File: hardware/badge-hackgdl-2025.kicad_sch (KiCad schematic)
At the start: 53 parts, among them J1 ADDON, J2 Battery, P1 USB_C_Plug_USB2.0, Q1 DMG3415U-7, Q2 MMBT2222A, SW1 ON, SW2 RESET, SW3 BOOT, SW4 RIGHT, SW5 BACK, SW6 LEFT, SW7 MIDDLE, U1 XC6220B331MR-G, U2 ESP32-S3-WROOM-1-N16

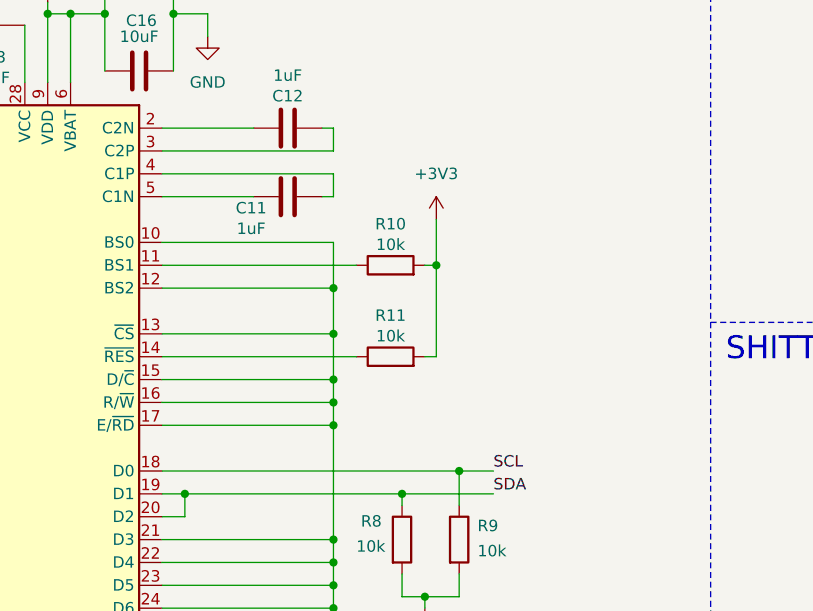
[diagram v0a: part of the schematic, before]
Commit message: feat(hw): add capacitor in reset pin
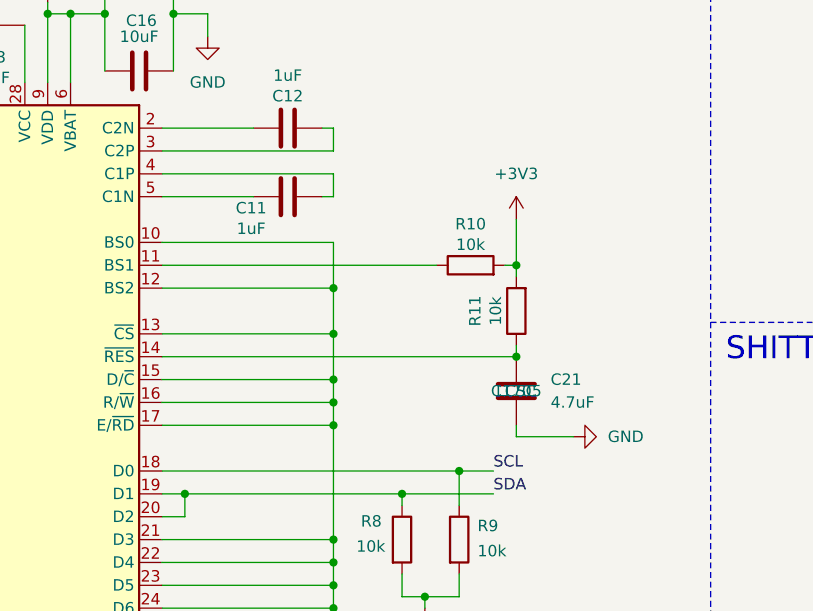
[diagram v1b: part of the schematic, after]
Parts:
- added C21: 4.7uF, Capacitor_SMD:C_0603_1608Metric, symbol Device:C
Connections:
- net GND: now also C21.2
- net at DS1.14 (~{RES}), R11.1: now also C21.1
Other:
- moved on the sheet: R10, R11
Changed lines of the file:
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@@
 	)
 	(junction
+		(at 93.98 129.54)
+		(diameter 0)
+		(color 0 0 0 0)
+	)
+	(junction
 		(at 229.87 96.52)
 		(diameter 0)
@@
 	)
 	(junction
-		(at 85.09 129.54)
-		(diameter 0)
-		(color 0 0 0 0)
-	)
-	(junction
 		(at 104.14 48.26)
 		(diameter 0)
@@
 	)
 	(junction
+		(at 93.98 139.7)
+		(diameter 0)
+		(color 0 0 0 0)
+	)
+	(junction
 		(at 41.91 190.5)
 		(diameter 0)
@@
 	(wire
 		(pts
+			(xy 93.98 129.54) (xy 93.98 130.81)
+		)
+		(stroke
+			(width 0)
+			(type default)
+		)
+	)
+	(wire
+		(pts
 			(xy 44.45 190.5) (xy 44.45 185.42)
 		)
@@
 	(wire
 		(pts
-			(xy 54.61 129.54) (xy 76.2 129.54)
+			(xy 54.61 129.54) (xy 85.09 129.54)
 		)
 		(stroke
@@
 	(wire
 		(pts
+			(xy 93.98 148.59) (xy 100.33 148.59)
+		)
+		(stroke
+			(width 0)
+			(type default)
+		)
+	)
+	(wire
+		(pts
 			(xy 78.74 46.99) (xy 78.74 45.72)
 		)
@@
 	(wire
 		(pts
-			(xy 85.09 129.54) (xy 83.82 129.54)
+			(xy 93.98 129.54) (xy 92.71 129.54)
 		)
 		(stroke
@@
 	(wire
 		(pts
-			(xy 85.09 124.46) (xy 85.09 129.54)
+			(xy 93.98 124.46) (xy 93.98 129.54)
 		)
 		(stroke
@@
 	(wire
 		(pts
-			(xy 54.61 139.7) (xy 76.2 139.7)
+			(xy 54.61 139.7) (xy 93.98 139.7)
 		)
 		(stroke
@@
 	(wire
 		(pts
+			(xy 93.98 138.43) (xy 93.98 139.7)
+		)
+		(stroke
+			(width 0)
+			(type default)
+		)
+	)
+	(wire
+		(pts
 			(xy 163.83 19.812) (xy 163.83 20.32)
 		)
@@
 	(wire
 		(pts
-			(xy 85.09 139.7) (xy 85.09 129.54)
-		)
-		(stroke
-			(width 0)
-			(type default)
-		)
-	)
-	(wire
-		(pts
 			(xy 54.61 147.32) (xy 73.66 147.32)
 		)
@@
 	(wire
 		(pts
-			(xy 83.82 139.7) (xy 85.09 139.7)
+			(xy 93.98 148.59) (xy 93.98 147.32)
 		)
 		(stroke
@@
 	(symbol
 		(lib_id "Device:R")
-		(at 80.01 139.7 90)
+		(at 93.98 134.62 180)
 		(unit 1)
 		(exclude_from_sim no)
@@
 		(dnp no)
 		(property "Reference" "R11"
-			(at 80.01 135.128 90)
+			(at 89.408 134.62 90)
 			(effects
 				(font
@@
 		)
 		(property "Value" "10k"
-			(at 80.01 137.414 90)
+			(at 91.694 134.62 90)
 			(effects
 				(font
@@
 		)
 		(property "Footprint" "Resistor_SMD:R_0603_1608Metric"
-			(at 80.01 141.478 90)
+			(at 95.758 134.62 90)
 			(effects
 				(font
@@
 		)
 		(property "Datasheet" "~"
-			(at 80.01 139.7 0)
+			(at 93.98 134.62 0)
 			(effects
 				(font
@@
 		)
 		(property "Description" "Resistor"
-			(at 80.01 139.7 0)
+			(at 93.98 134.62 0)
 			(effects
 				(font
@@
 		)
 		(property "LCSC#" "C99198"
-			(at 80.01 139.7 0)
+			(at 93.98 134.62 0)
 			(effects
 				(font
@@
 		)
 		(property "provedor" "LCSC"
-			(at 80.01 139.7 0)
+			(at 93.98 134.62 0)
 			(effects
 				(font
@@
 		(lib_name "+3V3_3")
 		(lib_id "power:+3V3")
-		(at 85.09 124.46 0)
+		(at 93.98 124.46 0)
 		(unit 1)
 		(exclude_from_sim no)
@@
 		(fields_autoplaced yes)
 		(property "Reference" "#PWR034"
-			(at 85.09 128.27 0)
+			(at 93.98 128.27 0)
 			(effects
 				(font
@@
 		)
 		(property "Value" "+3V3"
-			(at 85.09 119.38 0)
+			(at 93.98 119.38 0)
 			(effects
 				(font
@@
 		)
 		(property "Footprint" ""
-			(at 85.09 124.46 0)
+			(at 93.98 124.46 0)
 			(effects
 				(font
@@
 		)
 		(property "Datasheet" ""
-			(at 85.09 124.46 0)
+			(at 93.98 124.46 0)
 			(effects
 				(font
@@
 		)
 		(property "Description" "Power symbol creates a global label with name \"+3V3\""
-			(at 85.09 124.46 0)
+			(at 93.98 124.46 0)
 			(effects
 				(font
@@
 	)
 	(symbol
+		(lib_id "Device:C")
+		(at 93.98 143.51 0)
+		(unit 1)
+		(exclude_from_sim no)
+		(in_bom yes)
+		(on_board yes)
+		(dnp no)
+		(fields_autoplaced yes)
+		(property "Reference" "C21"
+			(at 97.79 142.2399 0)
+			(effects
+				(font
+					(size 1.27 1.27)
+				)
+				(justify left)
+			)
+		)
+		(property "Value" "4.7uF"
+			(at 97.79 144.7799 0)
+			(effects
+				(font
+					(size 1.27 1.27)
+				)
+				(justify left)
+			)
+		)
+		(property "Footprint" "Capacitor_SMD:C_0603_1608Metric"
+			(at 94.9452 147.32 0)
+			(effects
+				(font
+					(size 1.27 1.27)
+				)
+				(hide yes)
+			)
+		)
+		(property "Datasheet" "~"
+			(at 93.98 143.51 0)
+			(effects
+				(font
+					(size 1.27 1.27)
+				)
+				(hide yes)
+			)
+		)
+		(property "Description" "Unpolarized capacitor"
+			(at 93.98 143.51 0)
+			(effects
+				(font
+					(size 1.27 1.27)
+				)
+				(hide yes)
+			)
+		)
+		(property "LCSC#" "C1705"
+			(at 93.98 143.51 0)
+			(effects
+				(font
+					(size 1.27 1.27)
+				)
+			)
+		)
+		(property "provedor" "LCSC"
+			(at 93.98 143.51 0)
+			(effects
+				(font
+					(size 1.27 1.27)
+				)
+			)
+		)
+		(pin "2"
+		)
+		(pin "1"
+		)
+		(instances
+			(project ""
+				(path "/570c3069-5a6c-4b3e-98ab-959d221dff05"
+					(reference "C21")
+					(unit 1)
+				)
+			)
+		)
+	)
+	(symbol
 		(lib_id "power:GND")
 		(at 163.83 26.162 0)
@@
 	)
 	(symbol
+		(lib_name "GND_10")
+		(lib_id "power:GND")
+		(at 100.33 148.59 90)
+		(unit 1)
+		(exclude_from_sim no)
+		(in_bom yes)
+		(on_board yes)
+		(dnp no)
+		(fields_autoplaced yes)
+		(property "Reference" "#PWR049"
+			(at 106.68 148.59 0)
+			(effects
+				(font
+					(size 1.27 1.27)
+				)
+				(hide yes)
+			)
+		)
+		(property "Value" "GND"
+			(at 104.14 148.5899 90)
+			(effects
+				(font
+					(size 1.27 1.27)
+				)
+				(justify right)
+			)
+		)
+		(property "Footprint" ""
+			(at 100.33 148.59 0)
+			(effects
+				(font
+					(size 1.27 1.27)
+				)
+				(hide yes)
+			)
+		)
+		(property "Datasheet" ""
+			(at 100.33 148.59 0)
+			(effects
+				(font
+					(size 1.27 1.27)
+				)
+				(hide yes)
+			)
+		)
+		(property "Description" "Power symbol creates a global label with name \"GND\" , ground"
+			(at 100.33 148.59 0)
+			(effects
+				(font
+					(size 1.27 1.27)
+				)
+				(hide yes)
+			)
+		)
+		(pin "1"
+		)
+		(instances
+			(project ""
+				(path "/570c3069-5a6c-4b3e-98ab-959d221dff05"
+					(reference "#PWR049")
+					(unit 1)
+				)
+			)
+		)
+	)
+	(symbol
 		(lib_id "Device:C_Small")
 		(at 164.719 50.165 270)
@@
 	(symbol
 		(lib_id "Device:R")
-		(at 80.01 129.54 90)
+		(at 88.9 129.54 90)
 		(unit 1)
 		(exclude_from_sim no)
@@
 		(dnp no)
 		(property "Reference" "R10"
-			(at 80.01 124.968 90)
+			(at 88.9 124.968 90)
 			(effects
 				(font
@@
 		)
 		(property "Value" "10k"
-			(at 80.01 127.254 90)
+			(at 88.9 127.254 90)
 			(effects
 				(font
@@
 		)
 		(property "Footprint" "Resistor_SMD:R_0603_1608Metric"
-			(at 80.01 131.318 90)
+			(at 88.9 131.318 90)
 			(effects
 				(font
@@
 		)
 		(property "Datasheet" "~"
-			(at 80.01 129.54 0)
+			(at 88.9 129.54 0)
 			(effects
 				(font
@@
 		)
 		(property "Description" "Resistor"
-			(at 80.01 129.54 0)
+			(at 88.9 129.54 0)
 			(effects
 				(font
@@
 		)
 		(property "LCSC#" "C99198"
-			(at 80.01 129.54 0)
+			(at 88.9 129.54 0)
 			(effects
 				(font
@@
 		)
 		(property "provedor" "LCSC"
-			(at 80.01 129.54 0)
+			(at 88.9 129.54 0)
 			(effects
 				(font

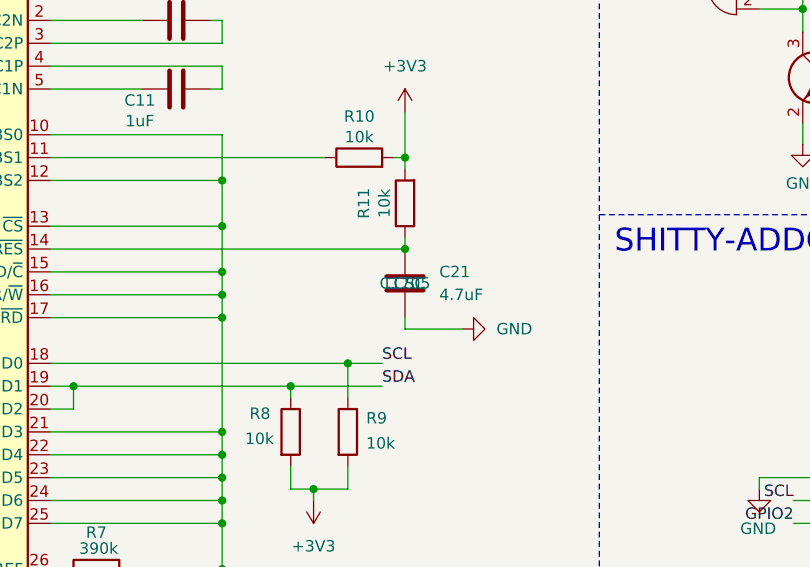
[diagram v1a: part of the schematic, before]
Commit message: feat(hw): add labels
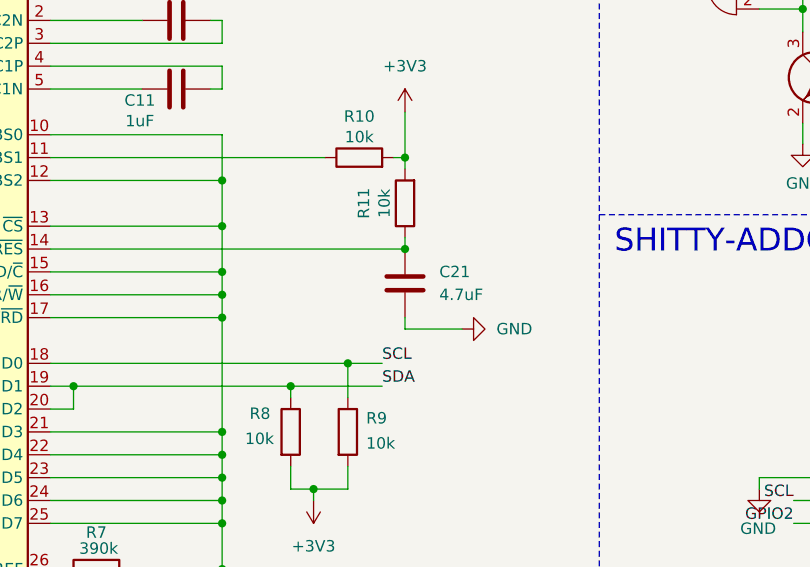
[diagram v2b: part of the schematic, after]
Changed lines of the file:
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@@
 					(size 1.27 1.27)
 				)
+				(hide yes)
 			)
 		)
 		(property "provedor" "LCSC"
-			(at 93.98 143.51 0)
+			(at 97.79 146.0499 0)
 			(effects
 				(font
 					(size 1.27 1.27)
 				)
+				(justify left)
+				(hide yes)
 			)
 		)

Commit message: feat(hw): update button
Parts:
- SW4, SW5, SW6, SW7: footprint Button_Switch_SMD:SW_SPST_TL3342 -> Footprints:Button_6.6x6.5; LCSC# C318884 -> C480263
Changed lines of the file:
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@@
 			)
 		)
-		(property "Footprint" "Button_Switch_SMD:SW_SPST_TL3342"
+		(property "Footprint" "Footprints:Button_6.6x6.5"
 			(at 237.49 83.82 0)
 			(effects
@@
 			)
 		)
-		(property "LCSC#" "C318884"
+		(property "LCSC#" "C480263"
 			(at 237.49 88.9 0)
 			(effects
@@
 			)
 		)
-		(property "Footprint" "Button_Switch_SMD:SW_SPST_TL3342"
+		(property "Footprint" "Footprints:Button_6.6x6.5"
 			(at 265.43 88.9 0)
 			(effects
@@
 			)
 		)
-		(property "LCSC#" "C318884"
+		(property "LCSC#" "C480263"
 			(at 265.43 93.98 0)
 			(effects
@@
 			)
 		)
-		(property "Footprint" "Button_Switch_SMD:SW_SPST_TL3342"
+		(property "Footprint" "Footprints:Button_6.6x6.5"
 			(at 236.22 104.14 0)
 			(effects
@@
 			)
 		)
-		(property "LCSC#" "C318884"
+		(property "LCSC#" "C480263"
 			(at 236.22 109.22 0)
 			(effects
@@
 			)
 		)
-		(property "Footprint" "Button_Switch_SMD:SW_SPST_TL3342"
+		(property "Footprint" "Footprints:Button_6.6x6.5"
 			(at 210.82 91.44 0)
 			(effects
@@
 			)
 		)
-		(property "LCSC#" "C318884"
+		(property "LCSC#" "C480263"
 			(at 210.82 96.52 0)
 			(effects

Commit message: feat(hw): change components in BOM
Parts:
- C10, C15, C17, C18, C19, C20, C6, C7, C8, C9: LCSC# C15725 -> C66501
- C11, C12, C3: LCSC# C15849 -> C696901
- R3: manf# RC0603DR-07100KL -> (none)
- R5: LCSC# C103661 -> C25241
- R6: LCSC# C110776 -> C21190; manf# RC0603JR-071K1L -> (none)
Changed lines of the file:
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@@
 			)
 		)
-		(property "LCSC#" "C15725"
+		(property "LCSC#" "C66501"
 			(at 52.07 97.79 0)
 			(effects
@@
 			)
 		)
-		(property "LCSC#" "C15725"
+		(property "LCSC#" "C66501"
 			(at 210.82 105.41 0)
 			(effects
@@
 			)
 		)
-		(property "LCSC#" "C15725"
+		(property "LCSC#" "C66501"
 			(at 265.43 101.6 0)
 			(effects
@@
 			)
 		)
-		(property "LCSC#" "C15849"
+		(property "LCSC#" "C696901"
 			(at 156.21 22.987 0)
 			(effects
@@
 			)
 		)
-		(property "LCSC#" "C15725"
+		(property "LCSC#" "C66501"
 			(at 165.1 69.85 0)
 			(effects
@@
 			)
 		)
-		(property "LCSC#" "C15725"
+		(property "LCSC#" "C66501"
 			(at 236.22 116.84 0)
 			(effects
@@
 			)
 		)
-		(property "manf#" "RC0603DR-07100KL"
+		(property "manf#" ""
 			(at 78.74 49.53 0)
 			(effects
@@
 			)
 		)
-		(property "LCSC#" "C15725"
+		(property "LCSC#" "C66501"
 			(at 269.24 135.89 0)
 			(effects
@@
 			)
 		)
-		(property "LCSC#" "C15849"
+		(property "LCSC#" "C696901"
 			(at 68.58 114.3 0)
 			(effects
@@
 			)
 		)
-		(property "LCSC#" "C15725"
+		(property "LCSC#" "C66501"
 			(at 164.719 50.165 0)
 			(effects
@@
 			)
 		)
-		(property "LCSC#" "C15725"
+		(property "LCSC#" "C66501"
 			(at 241.3 135.89 0)
 			(effects
@@
 			)
 		)
-		(property "LCSC#" "C110776"
+		(property "LCSC#" "C21190"
 			(at 152.908 120.65 0)
 			(effects
@@
 			)
 		)
-		(property "manf#" "RC0603JR-071K1L"
+		(property "manf#" ""
 			(at 152.908 120.65 0)
 			(effects
@@
 			)
 		)
-		(property "LCSC#" "C103661"
+		(property "LCSC#" "C25241"
 			(at 199.39 148.59 0)
 			(effects
@@
 			)
 		)
-		(property "LCSC#" "C15849"
+		(property "LCSC#" "C696901"
 			(at 68.58 121.92 0)
 			(effects
@@
 			)
 		)
-		(property "LCSC#" "C15725"
+		(property "LCSC#" "C66501"
 			(at 237.49 96.52 0)
 			(effects
@@
 			)
 		)
-		(property "LCSC#" "C15725"
+		(property "LCSC#" "C66501"
 			(at 219.71 135.89 0)
 			(effects

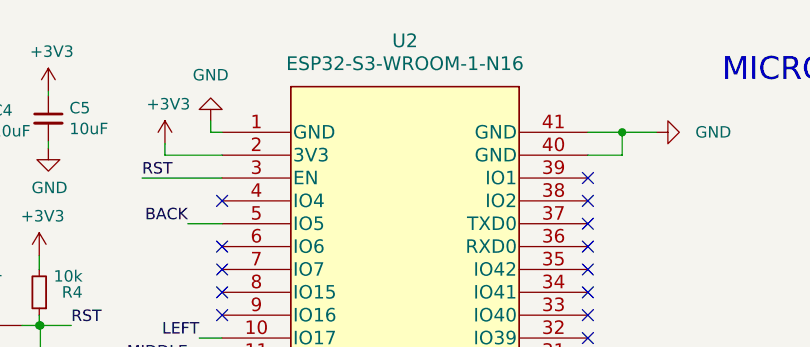
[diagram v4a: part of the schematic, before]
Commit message: refactor(hw): switch approached the edge of the pcb
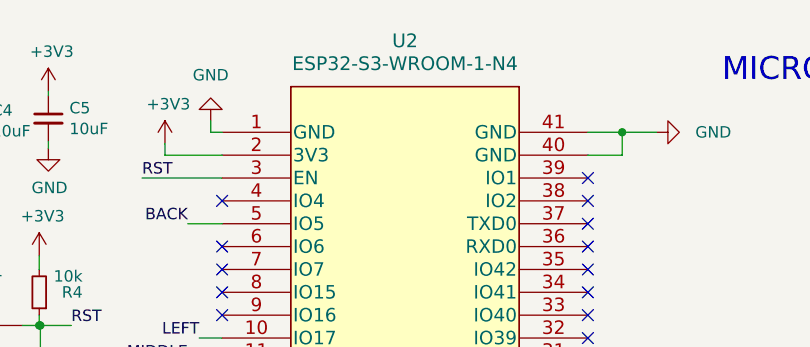
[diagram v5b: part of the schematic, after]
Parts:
- U2: value ESP32-S3-WROOM-1-N16 -> ESP32-S3-WROOM-1-N4
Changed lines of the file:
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@@
 			)
 		)
-		(property "Value" "ESP32-S3-WROOM-1-N16"
+		(property "Value" "ESP32-S3-WROOM-1-N4"
 			(at 212.09 16.51 0)
 			(effects

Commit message: feat(hw): update BOM
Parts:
- C1, C10, C11, C12, C13, C14, C15, C16, C17, C18, C19, C2, C20, C21, C3, C4, C5, C6, C7, C8, C9, D1, D2, D3, D4, D5, DS1, F1, J1, P1, Q1, Q2, R1, R10, R11, R2, R3, R4, R5, R6, R7, R8, R9, SW1, SW2, SW3, SW4, SW5, SW6, SW7, U1: provedor LCSC -> JLCPCB
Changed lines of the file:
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@@
 			)
 		)
-		(property "provedor" "LCSC"
+		(property "provedor" "JLCPCB"
 			(at 59.69 185.42 0)
 			(effects
@@
 			)
 		)
-		(property "provedor" "LCSC"
+		(property "provedor" "JLCPCB"
 			(at 52.07 97.79 0)
 			(effects
@@
 			)
 		)
-		(property "provedor" "LCSC"
+		(property "provedor" "JLCPCB"
 			(at 233.68 148.59 0)
 			(effects
@@
 			)
 		)
-		(property "provedor" "LCSC"
+		(property "provedor" "JLCPCB"
 			(at 41.91 147.32 0)
 			(effects
@@
 			)
 		)
-		(property "provedor" "LCSC"
+		(property "provedor" "JLCPCB"
 			(at 210.82 105.41 0)
 			(effects
@@
 			)
 		)
-		(property "provedor" "LCSC"
+		(property "provedor" "JLCPCB"
 			(at 259.08 148.59 0)
 			(effects
@@
 			)
 		)
-		(property "provedor" "LCSC"
+		(property "provedor" "JLCPCB"
 			(at 265.43 101.6 0)
 			(effects
@@
 			)
 		)
-		(property "provedor" "LCSC"
+		(property "provedor" "JLCPCB"
 			(at 50.8 34.29 0)
 			(effects
@@
 			)
 		)
-		(property "provedor" "LCSC"
+		(property "provedor" "JLCPCB"
 			(at 237.49 88.9 0)
 			(effects
@@
 			)
 		)
-		(property "provedor" "LCSC"
+		(property "provedor" "JLCPCB"
 			(at 156.21 22.987 0)
 			(effects
@@
 			)
 		)
-		(property "provedor" "LCSC"
+		(property "provedor" "JLCPCB"
 			(at 116.84 48.26 0)
 			(effects
@@
 			)
 		)
-		(property "provedor" "LCSC"
+		(property "provedor" "JLCPCB"
 			(at 165.1 69.85 0)
 			(effects
@@
 			)
 		)
-		(property "provedor" "LCSC"
+		(property "provedor" "JLCPCB"
 			(at 236.22 116.84 0)
 			(effects
@@
 			)
 		)
-		(property "provedor" "LCSC"
+		(property "provedor" "JLCPCB"
 			(at 172.466 22.606 0)
 			(effects
@@
 			)
 		)
-		(property "provedor" "LCSC"
+		(property "provedor" "JLCPCB"
 			(at 78.74 49.53 0)
 			(effects
@@
 			)
 		)
-		(property "provedor" "LCSC"
+		(property "provedor" "JLCPCB"
 			(at 81.28 160.02 0)
 			(effects
@@
 			)
 		)
-		(property "provedor" "LCSC"
+		(property "provedor" "JLCPCB"
 			(at 265.43 93.98 0)
 			(effects
@@
 			)
 		)
-		(property "provedor" "LCSC"
+		(property "provedor" "JLCPCB"
 			(at 269.24 135.89 0)
 			(effects
@@
 			)
 		)
-		(property "provedor" "LCSC"
+		(property "provedor" "JLCPCB"
 			(at 93.98 134.62 0)
 			(effects
@@
 			)
 		)
-		(property "provedor" "LCSC"
+		(property "provedor" "JLCPCB"
 			(at 236.22 109.22 0)
 			(effects
@@
 			)
 		)
-		(property "provedor" "LCSC"
+		(property "provedor" "JLCPCB"
 			(at 59.69 175.26 0)
 			(effects
@@
 			)
 		)
-		(property "provedor" "LCSC"
+		(property "provedor" "JLCPCB"
 			(at 210.82 96.52 0)
 			(effects
@@
 			)
 		)
-		(property "provedor" "LCSC"
+		(property "provedor" "JLCPCB"
 			(at 95.25 45.72 0)
 			(effects
@@
 			)
 		)
-		(property "provedor" "LCSC"
+		(property "provedor" "JLCPCB"
 			(at 125.73 49.53 0)
 			(effects
@@
 			)
 		)
-		(property "provedor" "LCSC"
+		(property "provedor" "JLCPCB"
 			(at 212.09 148.59 0)
 			(effects
@@
 			)
 		)
-		(property "provedor" "LCSC"
+		(property "provedor" "JLCPCB"
 			(at 171.45 41.91 0)
 			(effects
@@
 			)
 		)
-		(property "provedor" "LCSC"
+		(property "provedor" "JLCPCB"
 			(at 97.79 146.0499 0)
 			(effects
@@
 			)
 		)
-		(property "provedor" "LCSC"
+		(property "provedor" "JLCPCB"
 			(at 30.48 41.91 0)
 			(effects
@@
 			)
 		)
-		(property "provedor" "LCSC"
+		(property "provedor" "JLCPCB"
 			(at 86.36 39.37 0)
 			(effects
@@
 			)
 		)
-		(property "provedor" "LCSC"
+		(property "provedor" "JLCPCB"
 			(at 68.58 114.3 0)
 			(effects
@@
 			)
 		)
-		(property "provedor" "LCSC"
+		(property "provedor" "JLCPCB"
 			(at 164.719 50.165 0)
 			(effects
@@
 			)
 		)
-		(property "provedor" "LCSC"
+		(property "provedor" "JLCPCB"
 			(at 241.3 135.89 0)
 			(effects
@@
 			)
 		)
-		(property "provedor" "LCSC"
+		(property "provedor" "JLCPCB"
 			(at 152.908 120.65 0)
 			(effects
@@
 			)
 		)
-		(property "provedor" "LCSC"
+		(property "provedor" "JLCPCB"
 			(at 199.39 148.59 0)
 			(effects
@@
 			)
 		)
-		(property "provedor" "LCSC"
+		(property "provedor" "JLCPCB"
 			(at 52.07 107.95 0)
 			(effects
@@
 			)
 		)
-		(property "provedor" "LCSC"
+		(property "provedor" "JLCPCB"
 			(at 164.846 60.96 0)
 			(effects
@@
 			)
 		)
-		(property "provedor" "LCSC"
+		(property "provedor" "JLCPCB"
 			(at 138.176 109.474 0)
 			(effects
@@
 			)
 		)
-		(property "provedor" "LCSC"
+		(property "provedor" "JLCPCB"
 			(at 140.716 120.65 0)
 			(effects
@@
 			)
 		)
-		(property "provedor" "LCSC"
+		(property "provedor" "JLCPCB"
 			(at 147.32 167.64 0)
 			(effects
@@
 			)
 		)
-		(property "provedor" "LCSC"
+		(property "provedor" "JLCPCB"
 			(at 104.14 53.34 0)
 			(effects
@@
 			)
 		)
-		(property "provedor" "LCSC"
+		(property "provedor" "JLCPCB"
 			(at 88.9 129.54 0)
 			(effects
@@
 			)
 		)
-		(property "provedor" "LCSC"
+		(property "provedor" "JLCPCB"
 			(at 35.56 102.87 0)
 			(effects
@@
 			)
 		)
-		(property "provedor" "LCSC"
+		(property "provedor" "JLCPCB"
 			(at 53.34 26.67 0)
 			(effects
@@
 			)
 		)
-		(property "provedor" "LCSC"
+		(property "provedor" "JLCPCB"
 			(at 68.58 121.92 0)
 			(effects
@@
 			)
 		)
-		(property "provedor" "LCSC"
+		(property "provedor" "JLCPCB"
 			(at 87.63 160.02 0)
 			(effects
@@
 			)
 		)
-		(property "provedor" "LCSC"
+		(property "provedor" "JLCPCB"
 			(at 237.49 96.52 0)
 			(effects
@@
 			)
 		)
-		(property "provedor" "LCSC"
+		(property "provedor" "JLCPCB"
 			(at 50.8 31.75 0)
 			(effects
@@
 			)
 		)
-		(property "provedor" "LCSC"
+		(property "provedor" "JLCPCB"
 			(at 219.71 135.89 0)
 			(effects
@@
 			)
 		)
-		(property "provedor" "LCSC"
+		(property "provedor" "JLCPCB"
 			(at 163.83 22.86 0)
 			(effects
@@
 			)
 		)
-		(property "provedor" "LCSC"
+		(property "provedor" "JLCPCB"
 			(at 164.465 45.593 0)
 			(effects
@@
 			)
 		)
-		(property "provedor" "LCSC"
+		(property "provedor" "JLCPCB"
 			(at 83.82 45.72 0)
 			(effects
